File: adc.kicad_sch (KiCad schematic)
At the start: 8 parts, among them U1 ADC3544, Y2 SiT9501

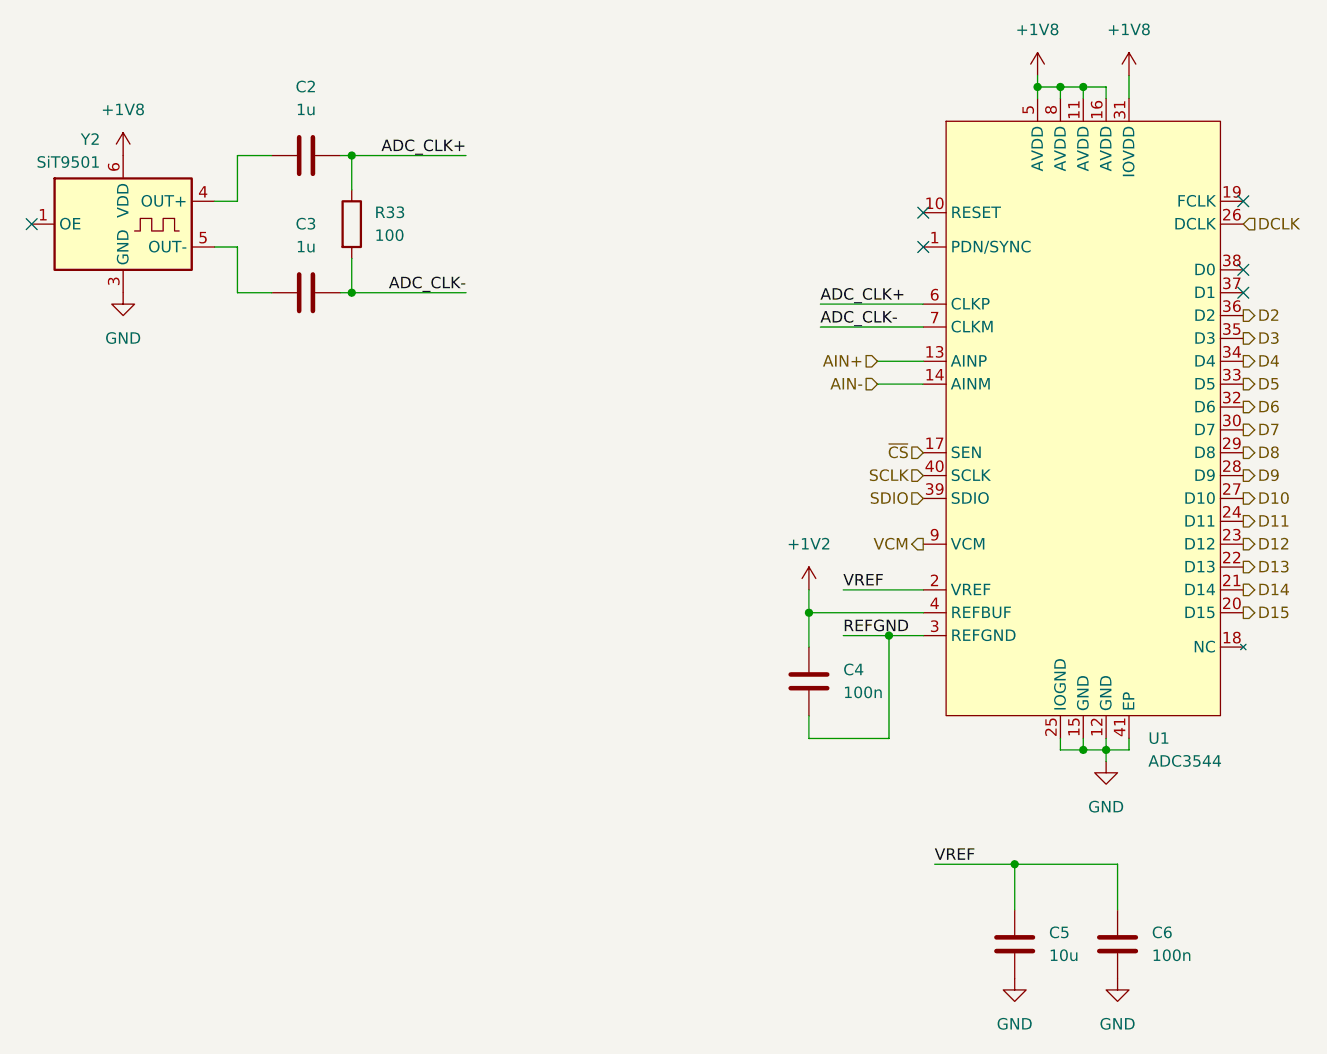
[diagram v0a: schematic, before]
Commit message: Fix SPI voltages, etc
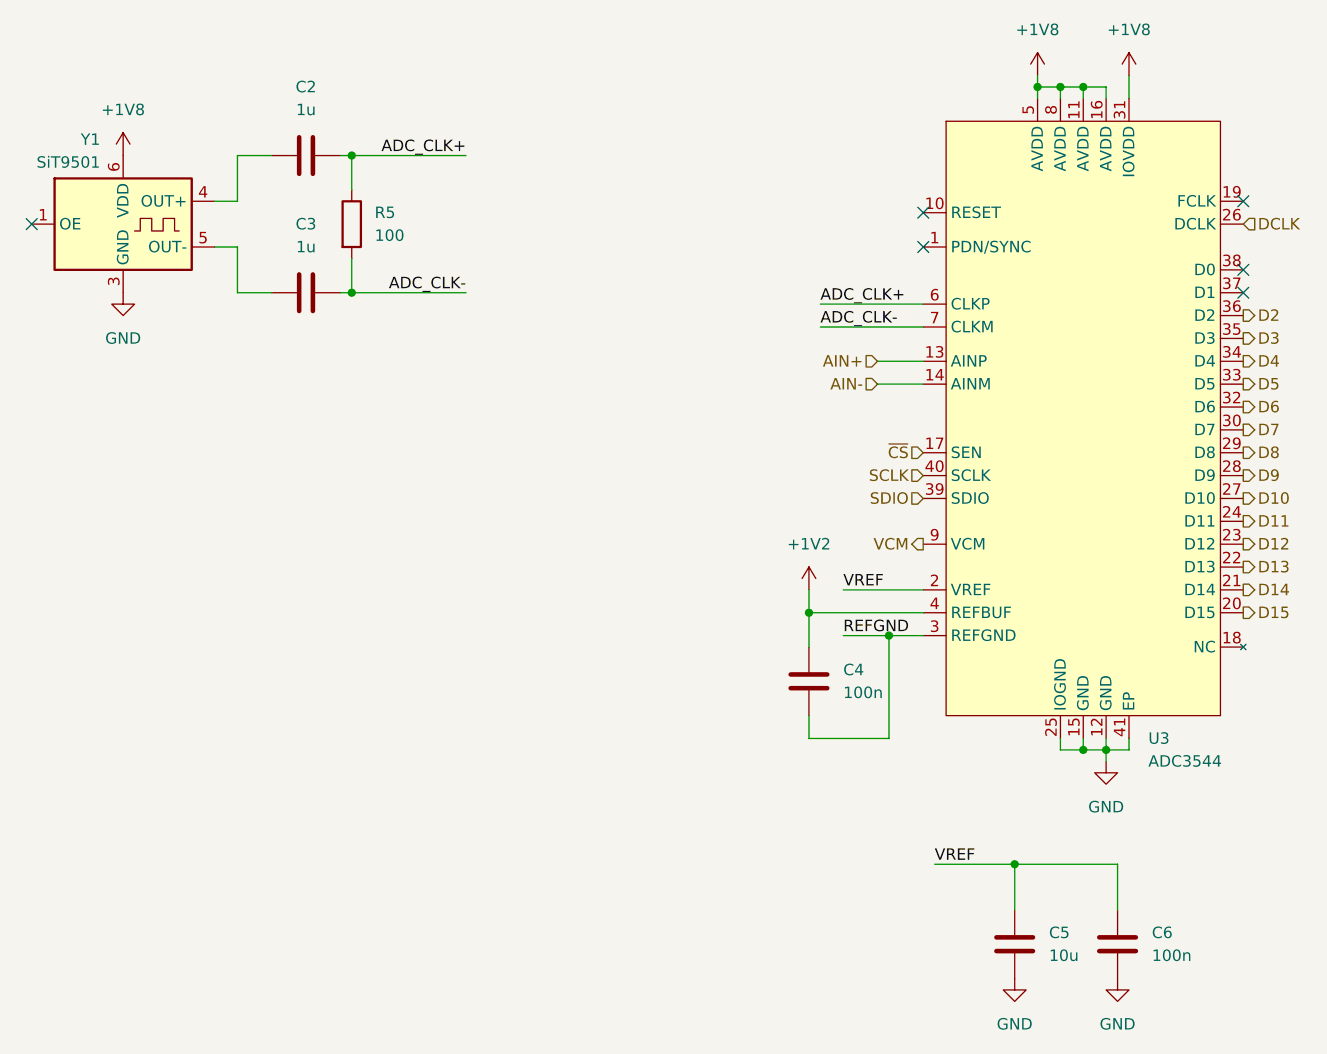
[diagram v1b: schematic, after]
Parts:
- renumbered R33 to R5, U1 to U3, Y2 to Y1
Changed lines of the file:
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@@
 		(dnp no)
 		(fields_autoplaced yes)
-		(property "Reference" "R33"
+		(property "Reference" "R5"
 			(at 173.99 62.2299 0)
 			(effects
@@
 			(project ""
 				(path "/c130ee0c-52ab-4414-8ea8-abd1a940c0be/e77cb95e-cf45-4364-b2d7-ac1345e04450"
-					(reference "R33")
+					(reference "R5")
 					(unit 1)
 				)
@@
 		(dnp no)
 		(fields_autoplaced yes)
-		(property "Reference" "#PWR06"
+		(property "Reference" "#PWR018"
 			(at 222.25 107.95 0)
 			(effects
@@
 			(project ""
 				(path "/c130ee0c-52ab-4414-8ea8-abd1a940c0be/e77cb95e-cf45-4364-b2d7-ac1345e04450"
-					(reference "#PWR06")
+					(reference "#PWR018")
 					(unit 1)
 				)
@@
 		(dnp no)
 		(fields_autoplaced yes)
-		(property "Reference" "#PWR010"
+		(property "Reference" "#PWR022"
 			(at 256.54 153.67 0)
 			(effects
@@
 			(project "usb3-sdr"
 				(path "/c130ee0c-52ab-4414-8ea8-abd1a940c0be/e77cb95e-cf45-4364-b2d7-ac1345e04450"
-					(reference "#PWR010")
+					(reference "#PWR022")
 					(unit 1)
 				)
@@
 		(dnp no)
 		(fields_autoplaced yes)
-		(property "Reference" "U1"
+		(property "Reference" "U3"
 			(at 259.9533 120.65 0)
 			(effects
@@
 			(project ""
 				(path "/c130ee0c-52ab-4414-8ea8-abd1a940c0be/e77cb95e-cf45-4364-b2d7-ac1345e04450"
-					(reference "U1")
+					(reference "U3")
 					(unit 1)
 				)
@@
 		(dnp no)
 		(fields_autoplaced yes)
-		(property "Reference" "#PWR07"
+		(property "Reference" "#PWR019"
 			(at 245.11 153.67 0)
 			(effects
@@
 			(project ""
 				(path "/c130ee0c-52ab-4414-8ea8-abd1a940c0be/e77cb95e-cf45-4364-b2d7-ac1345e04450"
-					(reference "#PWR07")
+					(reference "#PWR019")
 					(unit 1)
 				)
@@
 		(on_board yes)
 		(dnp no)
-		(property "Reference" "Y2"
+		(property "Reference" "Y1"
 			(at 143.51 54.102 0)
 			(effects
@@
 			(project ""
 				(path "/c130ee0c-52ab-4414-8ea8-abd1a940c0be/e77cb95e-cf45-4364-b2d7-ac1345e04450"
-					(reference "Y2")
+					(reference "Y1")
 					(unit 1)
 				)
@@
 		(dnp no)
 		(fields_autoplaced yes)
-		(property "Reference" "#PWR08"
+		(property "Reference" "#PWR020"
 			(at 247.65 50.8 0)
 			(effects
@@
 			(project "usb3-sdr"
 				(path "/c130ee0c-52ab-4414-8ea8-abd1a940c0be/e77cb95e-cf45-4364-b2d7-ac1345e04450"
-					(reference "#PWR08")
+					(reference "#PWR020")
 					(unit 1)
 				)
@@
 		(dnp no)
 		(fields_autoplaced yes)
-		(property "Reference" "#PWR09"
+		(property "Reference" "#PWR021"
 			(at 255.27 129.54 0)
 			(effects
@@
 			(project ""
 				(path "/c130ee0c-52ab-4414-8ea8-abd1a940c0be/e77cb95e-cf45-4364-b2d7-ac1345e04450"
-					(reference "#PWR09")
+					(reference "#PWR021")
 					(unit 1)
 				)
@@
 		(dnp no)
 		(fields_autoplaced yes)
-		(property "Reference" "#PWR0131"
+		(property "Reference" "#PWR016"
 			(at 146.05 59.69 0)
 			(effects
@@
 			(project ""
 				(path "/c130ee0c-52ab-4414-8ea8-abd1a940c0be/e77cb95e-cf45-4364-b2d7-ac1345e04450"
-					(reference "#PWR0131")
+					(reference "#PWR016")
 					(unit 1)
 				)
@@
 		(dnp no)
 		(fields_autoplaced yes)
-		(property "Reference" "#PWR011"
+		(property "Reference" "#PWR023"
 			(at 257.81 50.8 0)
 			(effects
@@
 			(project ""
 				(path "/c130ee0c-52ab-4414-8ea8-abd1a940c0be/e77cb95e-cf45-4364-b2d7-ac1345e04450"
-					(reference "#PWR011")
+					(reference "#PWR023")
 					(unit 1)
 				)
@@
 		(dnp no)
 		(fields_autoplaced yes)
-		(property "Reference" "#PWR0132"
+		(property "Reference" "#PWR017"
 			(at 146.05 77.47 0)
 			(effects
@@
 			(project ""
 				(path "/c130ee0c-52ab-4414-8ea8-abd1a940c0be/e77cb95e-cf45-4364-b2d7-ac1345e04450"
-					(reference "#PWR0132")
-					(unit 1)
-				)
+					(reference "#PWR017")
+					(unit 1)
+				)

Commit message: Fix ferrite, etc
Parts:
- renumbered C6 to C10, C2 to C6, C3 to C7, C4 to C8, C5 to C9, R5 to R7
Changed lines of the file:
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@@
 		(dnp no)
 		(fields_autoplaced yes)
-		(property "Reference" "C2"
+		(property "Reference" "C6"
 			(at 166.37 48.26 90)
 			(effects
@@
 			(project ""
 				(path "/c130ee0c-52ab-4414-8ea8-abd1a940c0be/e77cb95e-cf45-4364-b2d7-ac1345e04450"
-					(reference "C2")
+					(reference "C6")
 					(unit 1)
 				)
@@
 		(dnp no)
 		(fields_autoplaced yes)
-		(property "Reference" "C5"
+		(property "Reference" "C9"
 			(at 248.92 142.2399 0)
 			(effects
@@
 			(project ""
 				(path "/c130ee0c-52ab-4414-8ea8-abd1a940c0be/e77cb95e-cf45-4364-b2d7-ac1345e04450"
-					(reference "C5")
+					(reference "C9")
 					(unit 1)
 				)
@@
 		(dnp no)
 		(fields_autoplaced yes)
-		(property "Reference" "R5"
+		(property "Reference" "R7"
 			(at 173.99 62.2299 0)
 			(effects
@@
 			(project ""
 				(path "/c130ee0c-52ab-4414-8ea8-abd1a940c0be/e77cb95e-cf45-4364-b2d7-ac1345e04450"
-					(reference "R5")
+					(reference "R7")
 					(unit 1)
 				)
@@
 		(dnp no)
 		(fields_autoplaced yes)
-		(property "Reference" "#PWR018"
+		(property "Reference" "#PWR026"
 			(at 222.25 107.95 0)
 			(effects
@@
 			(project ""
 				(path "/c130ee0c-52ab-4414-8ea8-abd1a940c0be/e77cb95e-cf45-4364-b2d7-ac1345e04450"
-					(reference "#PWR018")
+					(reference "#PWR026")
 					(unit 1)
 				)
@@
 		(dnp no)
 		(fields_autoplaced yes)
-		(property "Reference" "#PWR022"
+		(property "Reference" "#PWR030"
 			(at 256.54 153.67 0)
 			(effects
@@
 			(project "usb3-sdr"
 				(path "/c130ee0c-52ab-4414-8ea8-abd1a940c0be/e77cb95e-cf45-4364-b2d7-ac1345e04450"
-					(reference "#PWR022")
+					(reference "#PWR030")
 					(unit 1)
 				)
@@
 		(dnp no)
 		(fields_autoplaced yes)
-		(property "Reference" "#PWR019"
+		(property "Reference" "#PWR027"
 			(at 245.11 153.67 0)
 			(effects
@@
 			(project ""
 				(path "/c130ee0c-52ab-4414-8ea8-abd1a940c0be/e77cb95e-cf45-4364-b2d7-ac1345e04450"
-					(reference "#PWR019")
+					(reference "#PWR027")
 					(unit 1)
 				)
@@
 		(dnp no)
 		(fields_autoplaced yes)
-		(property "Reference" "C3"
+		(property "Reference" "C7"
 			(at 166.37 63.5 90)
 			(effects
@@
 			(project "usb3-sdr"
 				(path "/c130ee0c-52ab-4414-8ea8-abd1a940c0be/e77cb95e-cf45-4364-b2d7-ac1345e04450"
-					(reference "C3")
+					(reference "C7")
 					(unit 1)
 				)
@@
 		(dnp no)
 		(fields_autoplaced yes)
-		(property "Reference" "#PWR020"
+		(property "Reference" "#PWR028"
 			(at 247.65 50.8 0)
 			(effects
@@
 			(project "usb3-sdr"
 				(path "/c130ee0c-52ab-4414-8ea8-abd1a940c0be/e77cb95e-cf45-4364-b2d7-ac1345e04450"
-					(reference "#PWR020")
+					(reference "#PWR028")
 					(unit 1)
 				)
@@
 		(dnp no)
 		(fields_autoplaced yes)
-		(property "Reference" "#PWR021"
+		(property "Reference" "#PWR029"
 			(at 255.27 129.54 0)
 			(effects
@@
 			(project ""
 				(path "/c130ee0c-52ab-4414-8ea8-abd1a940c0be/e77cb95e-cf45-4364-b2d7-ac1345e04450"
-					(reference "#PWR021")
+					(reference "#PWR029")
 					(unit 1)
 				)
@@
 		(dnp no)
 		(fields_autoplaced yes)
-		(property "Reference" "#PWR016"
+		(property "Reference" "#PWR024"
 			(at 146.05 59.69 0)
 			(effects
@@
 			(project ""
 				(path "/c130ee0c-52ab-4414-8ea8-abd1a940c0be/e77cb95e-cf45-4364-b2d7-ac1345e04450"
-					(reference "#PWR016")
+					(reference "#PWR024")
 					(unit 1)
 				)
@@
 		(dnp no)
 		(fields_autoplaced yes)
-		(property "Reference" "C6"
+		(property "Reference" "C10"
 			(at 260.35 142.2399 0)
 			(effects
@@
 			(project "usb3-sdr"
 				(path "/c130ee0c-52ab-4414-8ea8-abd1a940c0be/e77cb95e-cf45-4364-b2d7-ac1345e04450"
-					(reference "C6")
+					(reference "C10")
 					(unit 1)
 				)
@@
 		(dnp no)
 		(fields_autoplaced yes)
-		(property "Reference" "#PWR023"
+		(property "Reference" "#PWR031"
 			(at 257.81 50.8 0)
 			(effects
@@
 			(project ""
 				(path "/c130ee0c-52ab-4414-8ea8-abd1a940c0be/e77cb95e-cf45-4364-b2d7-ac1345e04450"
-					(reference "#PWR023")
+					(reference "#PWR031")
 					(unit 1)
 				)
@@
 		(dnp no)
 		(fields_autoplaced yes)
-		(property "Reference" "C4"
+		(property "Reference" "C8"
 			(at 226.06 113.0299 0)
 			(effects
@@
 			(project ""
 				(path "/c130ee0c-52ab-4414-8ea8-abd1a940c0be/e77cb95e-cf45-4364-b2d7-ac1345e04450"
-					(reference "C4")
+					(reference "C8")
 					(unit 1)
 				)
@@
 		(dnp no)
 		(fields_autoplaced yes)
-		(property "Reference" "#PWR017"
+		(property "Reference" "#PWR025"
 			(at 146.05 77.47 0)
 			(effects
@@
 			(project ""
 				(path "/c130ee0c-52ab-4414-8ea8-abd1a940c0be/e77cb95e-cf45-4364-b2d7-ac1345e04450"
-					(reference "#PWR017")
-					(unit 1)
-				)
+					(reference "#PWR025")
+					(unit 1)
+				)
